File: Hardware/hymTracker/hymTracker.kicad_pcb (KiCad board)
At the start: 2 copper layers, 45.7 x 54.6 mm, 19 parts, among them J1 DB9_Female, Q1 2N7000, U1 MP1584_DCDC, U2 GY-NEO6MV2

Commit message: panel.. callsign and RULER added
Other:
- outline, holes or cut-outs redrawn
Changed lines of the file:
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@@
   (general
     (thickness 1.6)
-    (drawings 16)
+    (drawings 20)
     (tracks 352)
     (zones 0)
@@
     )
   )
+  (gr_circle (center 96 71.15) (end 96 72.42) (layer Edge.Cuts) (width 0.05))
+  (gr_circle (center 66.32 71.1) (end 66.32 72.37) (layer Edge.Cuts) (width 0.05))
+  (gr_circle (center 96 51.05) (end 96 52.32) (layer Edge.Cuts) (width 0.05))
+  (gr_circle (center 66.3 51.05) (end 66.3 52.32) (layer Edge.Cuts) (width 0.05))
   (gr_text "TAMSAT\nhymTracker" (at 89.408 51.816) (layer B.Cu)
     (effects (font (size 1.5 1.5) (thickness 0.3)) (justify mirror))

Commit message: re-branding
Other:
- board text added: "TAMSAT iZCi"
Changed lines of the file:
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@@
   (general
     (thickness 1.6)
-    (drawings 20)
+    (drawings 22)
     (tracks 352)
     (zones 0)
@@
       (outputformat 1)
       (mirror false)
-      (drillshape 1)
+      (drillshape 0)
       (scaleselection 1)
-      (outputdirectory ""))
+      (outputdirectory "Gerber2/"))
   )
   (net 0 "")
@@
     )
   )
+  (gr_text "TAMSAT\niZCi" (at 68.58 91.44) (layer B.Cu)
+    (effects (font (size 1.5 1.5) (thickness 0.3)) (justify mirror))
+  )
+  (gr_text "TAMSAT\niZCi" (at 68.58 91.44) (layer F.Cu)
+    (effects (font (size 1.5 1.5) (thickness 0.3)))
+  )
   (gr_circle (center 96 71.15) (end 96 72.42) (layer Edge.Cuts) (width 0.05))

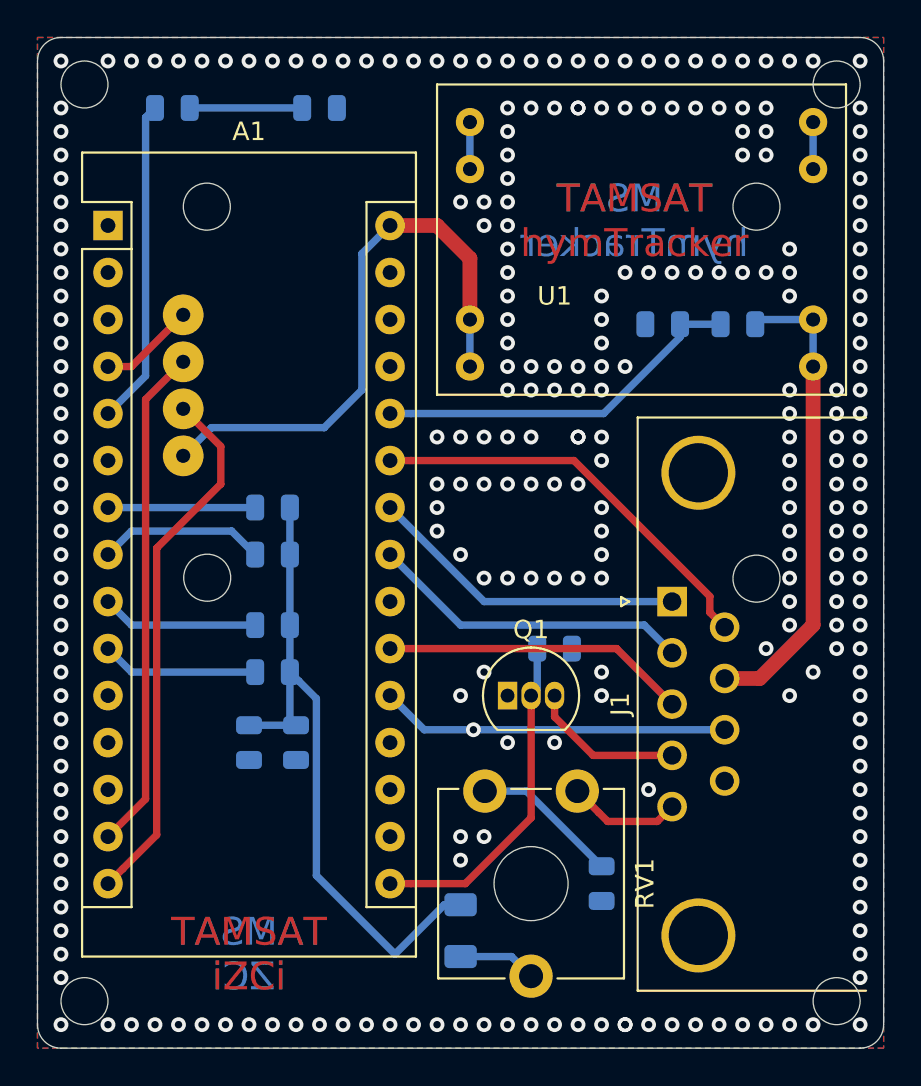
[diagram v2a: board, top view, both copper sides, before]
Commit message: R805->R1206 (small)
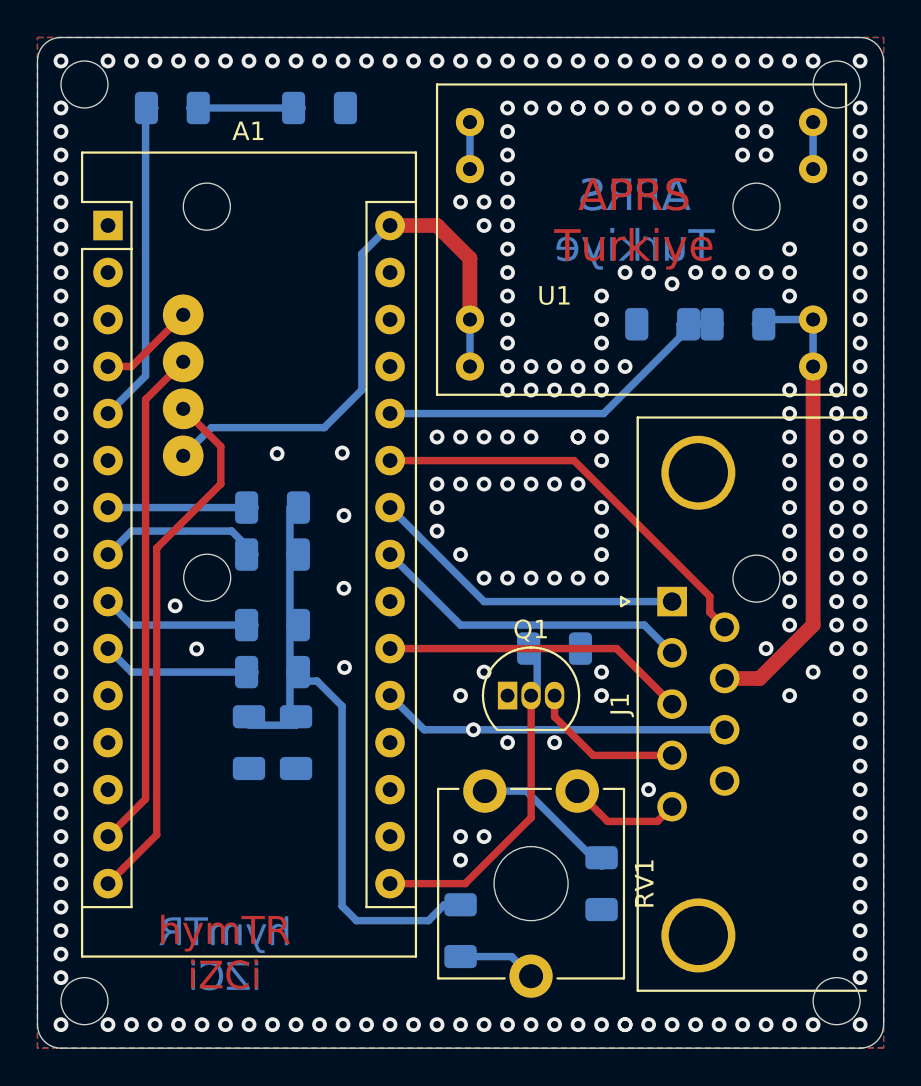
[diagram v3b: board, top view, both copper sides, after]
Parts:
- C1: footprint Capacitor_SMD:C_0805_2012Metric -> Capacitor_SMD:C_1206_3216Metric
- D1: footprint LED_SMD:LED_0805_2012Metric -> LED_SMD:LED_1206_3216Metric
- R1, R10, R2, R3, R4, R5, R6, R7, R8, R9: footprint Resistor_SMD:R_0805_2012Metric -> Resistor_SMD:R_1206_3216Metric
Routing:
- net Net-(C1-Pad1): track 36.7 -> 35.9 mm
- net GND: vias 248 -> 262
- net (no net): vias 13 -> 6
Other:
- board text added: "APRS Turkiye"
- board text added: "hymTR iZCi"
- board text removed: "TAMSAT hymTracker"
- board text removed: "TAMSAT iZCi"
